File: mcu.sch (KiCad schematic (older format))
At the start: 37 parts, among them J10 DX07S016JA1R1500, J11 Conn_02x08_Odd_Even, J7 PD8-15 (digital), J8 PA0-7 (analog), J9 debug, U3 STM32F407VETx, Y1 8Mhz

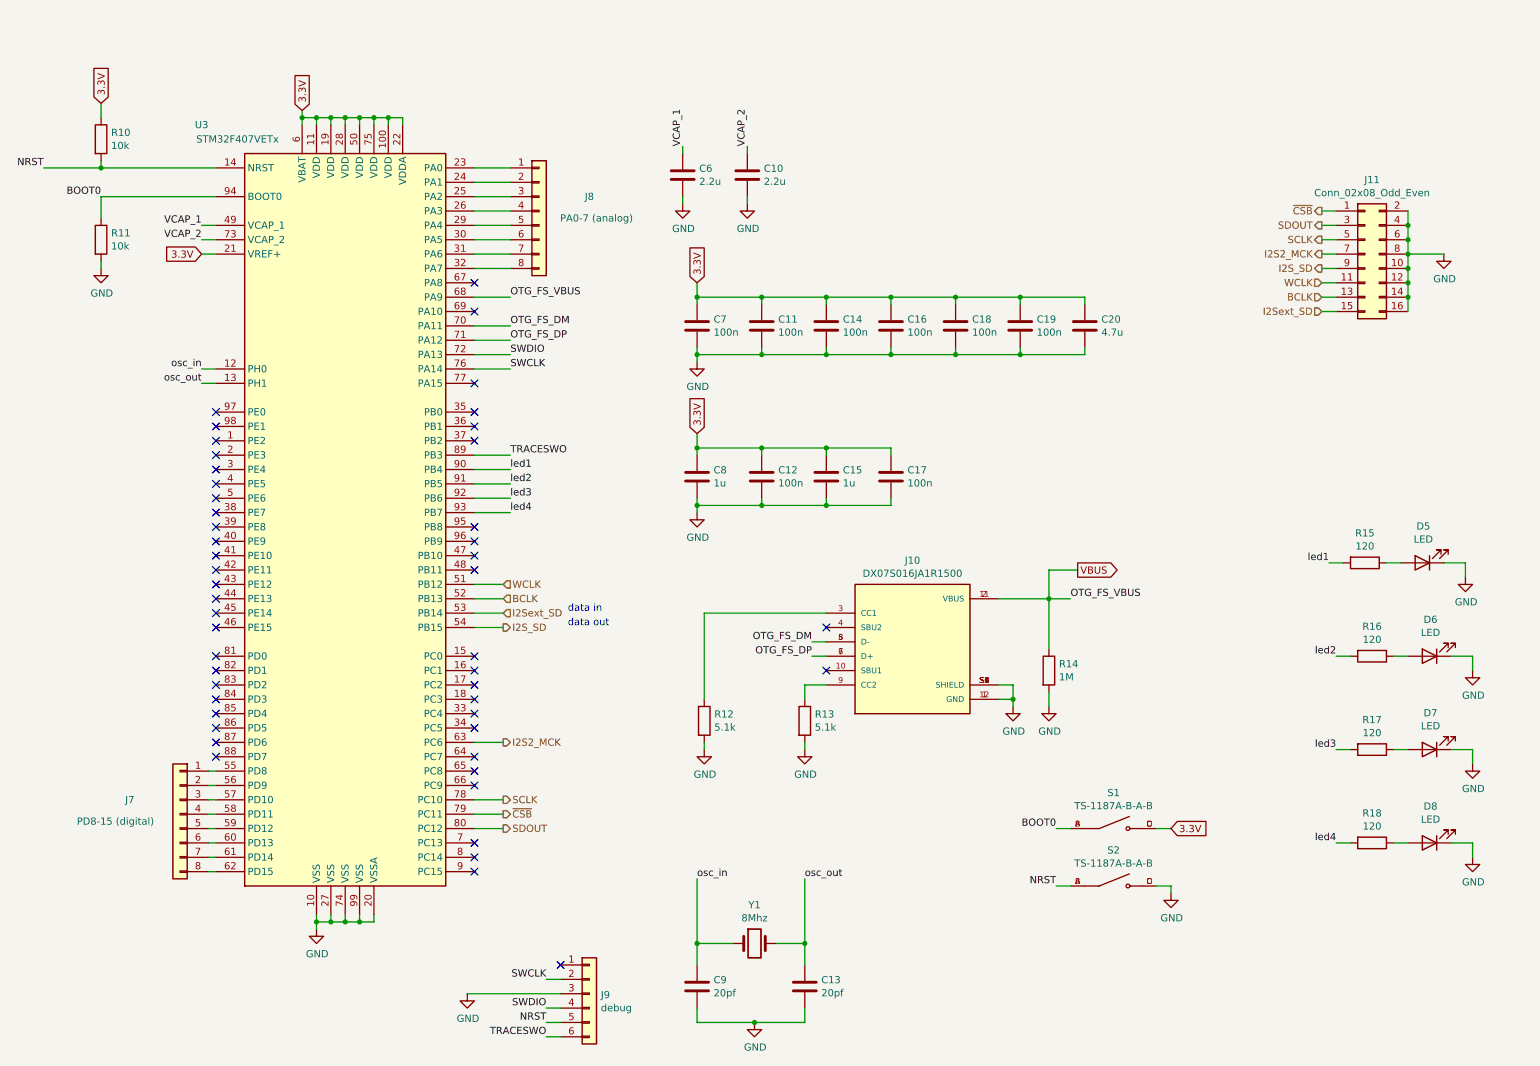
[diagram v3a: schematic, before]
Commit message: mcu.sch: replace microcontroller with SAME51J
The I2S bus is placed according to IOSET 1.

The ADC inputs are sprinkled around mostly-arbitrarily, but since
PA00-01 are not connected to either ADC peripheral, this uses PB08-09
for those two signals.  PB08 and 09 are connected to *both* ADCs, so
they should be sampleable simultaneously if necessary.
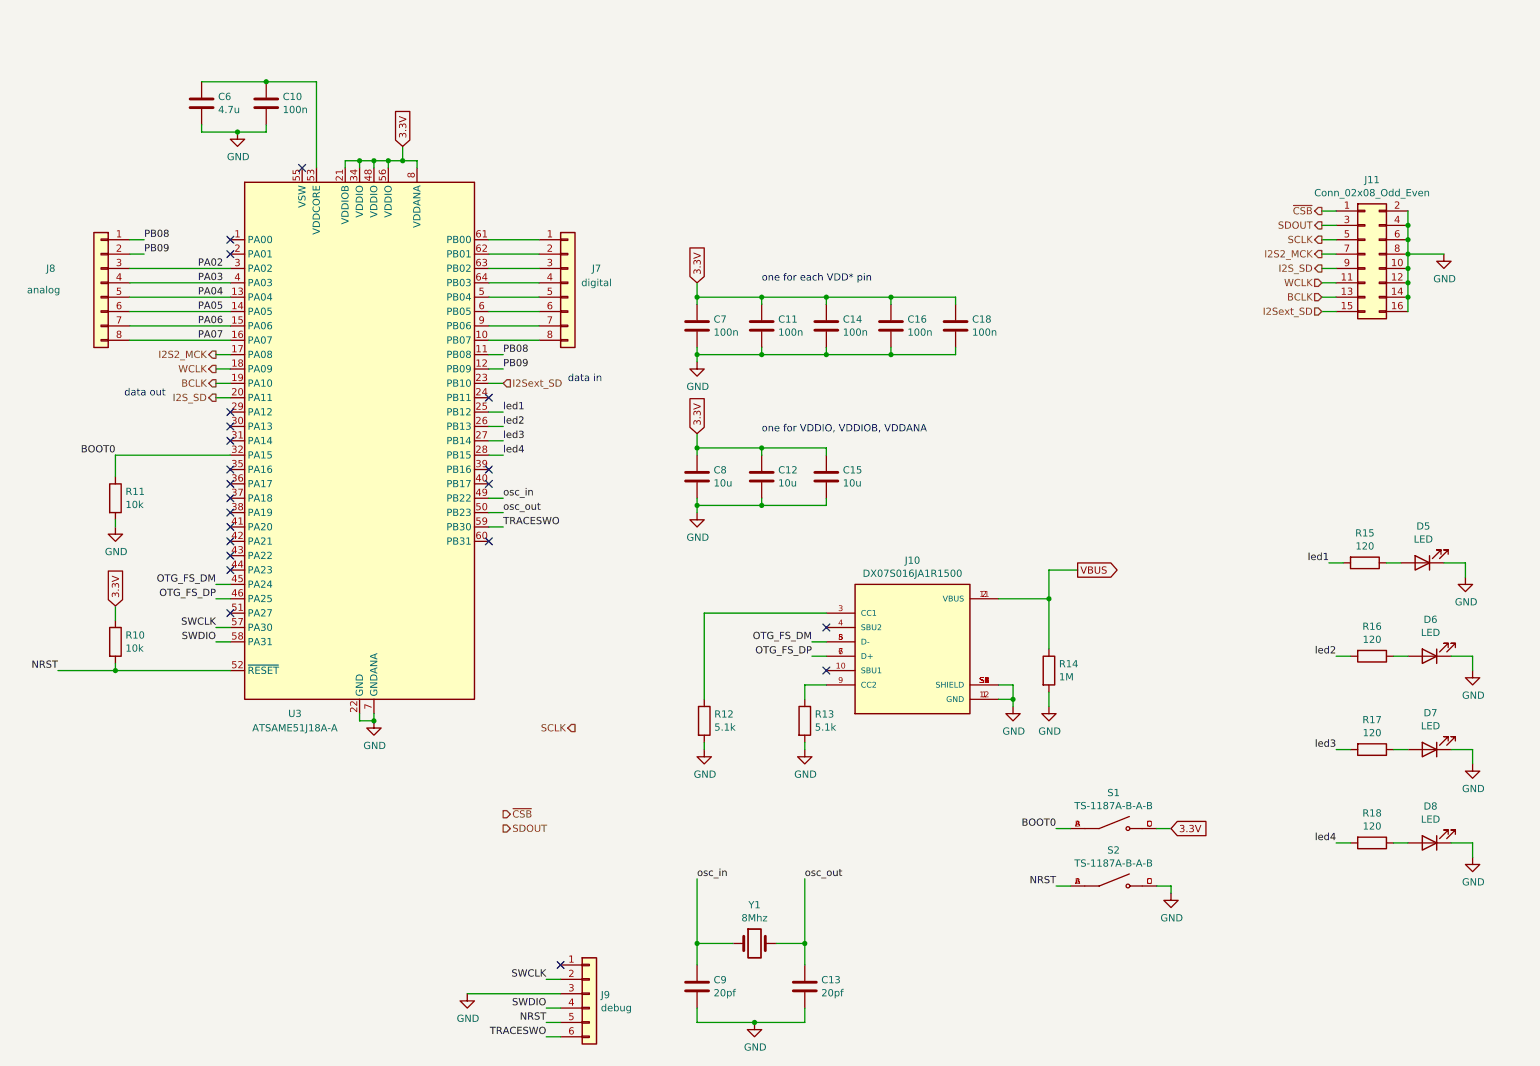
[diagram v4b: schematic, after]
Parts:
- removed C17, C19: 100n, Capacitor_SMD:C_0603_1608Metric, symbol Device:C
- removed C20: 4.7u, Capacitor_SMD:C_0603_1608Metric, symbol Device:C
- removed U3: STM32F407VETx, Package_QFP:LQFP-100_14x14mm_P0.5mm, symbol MCU_ST_STM32F4:STM32F407VETx
- added U3: ATSAME51J18A-A, Package_QFP:TQFP-64_10x10mm_P0.5mm, symbol MCU_Microchip_SAME:ATSAME51J18A-A
- C10: value 2.2u -> 100n; footprint Capacitor_SMD:C_0603_1608Metric -> (none)
- C12: value 100n -> 10u
- C15, C8: value 1u -> 10u
- C6: value 2.2u -> 4.7u; footprint Capacitor_SMD:C_0603_1608Metric -> (none)
- J7: value PD8-15 (digital) -> digital
- J8: value PA0-7 (analog) -> analog
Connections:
- net VCAP_2 is gone; now on an unnamed net: C10.1
- net 3.3V: now also U3.21 (VDDIOB), U3.34 (VDDIO), U3.48 (VDDIO), U3.56 (VDDIO), U3.8 (VDDANA)
- net BCLK: now also U3.19 (PA10)
- net BOOT0: now also U3.32 (PA15)
- net GND: now also U3.22 (GND), U3.33 (GND), U3.47 (GND), U3.54 (GND), U3.7 (GNDANA)
- net I2S2_MCK: now also U3.17 (PA08)
- net I2S_SD: now also U3.20 (PA11)
- net I2Sext_SD: now also U3.23 (PB10)
- net NRST: now also U3.52 (~RESET)
- net OTG_FS_DM: now also U3.45 (PA24)
- net OTG_FS_DP: now also U3.46 (PA25)
- net SWCLK: now also U3.57 (PA30)
- net SWDIO: now also U3.58 (PA31)
- net TRACESWO: now also U3.59 (PB30)
- net WCLK: now also U3.18 (PA09)
- net led1: now also U3.25 (PB12)
- net led2: now also U3.26 (PB13)
- net led3: now also U3.27 (PB14)
- net led4: now also U3.28 (PB15)
- net osc_in: now also U3.49 (PB22)
- net osc_out: now also U3.50 (PB23)
- net PB08: now reaches J8.1 (Pin_1)
- net PB08: now also U3.11 (PB08)
- net PB09: now reaches J8.2 (Pin_2)
- net PB09: now also U3.12 (PB09)
- net PA02: now reaches J8.3 (Pin_3)
- net PA02: now also U3.3 (PA02)
- net PA03: now reaches J8.4 (Pin_4)
- net PA03: now also U3.4 (PA03)
- net PA04: now reaches J8.5 (Pin_5)
- net PA04: now also U3.13 (PA04)
- net PA05: now reaches J8.6 (Pin_6)
- net PA05: now also U3.14 (PA05)
- net PA06: now reaches J8.7 (Pin_7)
- net PA06: now also U3.15 (PA06)
- net PA07: now reaches J8.8 (Pin_8)
- net PA07: now also U3.16 (PA07)
- net at J7.1 (Pin_1): now also U3.61 (PB00)
- net at J7.2 (Pin_2): now also U3.62 (PB01)
- net at J7.3 (Pin_3): now also U3.63 (PB02)
- net at J7.4 (Pin_4): now also U3.64 (PB03)
- net at J7.5 (Pin_5): now also U3.5 (PB04)
- net at J7.6 (Pin_6): now also U3.6 (PB05)
- net at J7.7 (Pin_7): now also U3.9 (PB06)
- net at J7.8 (Pin_8): now also U3.10 (PB07)
- net VCAP_1: no longer names the net of C6.1
- net VCAP_1: now also U3.53 (VDDCORE)
- no-connect marks 49 -> 22
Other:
- note added: "one for VDDIO, VDDIOB, VDDANA"
- note added: "one for each VDD* pin"
- moved on the sheet: J7, J8, R10, R11

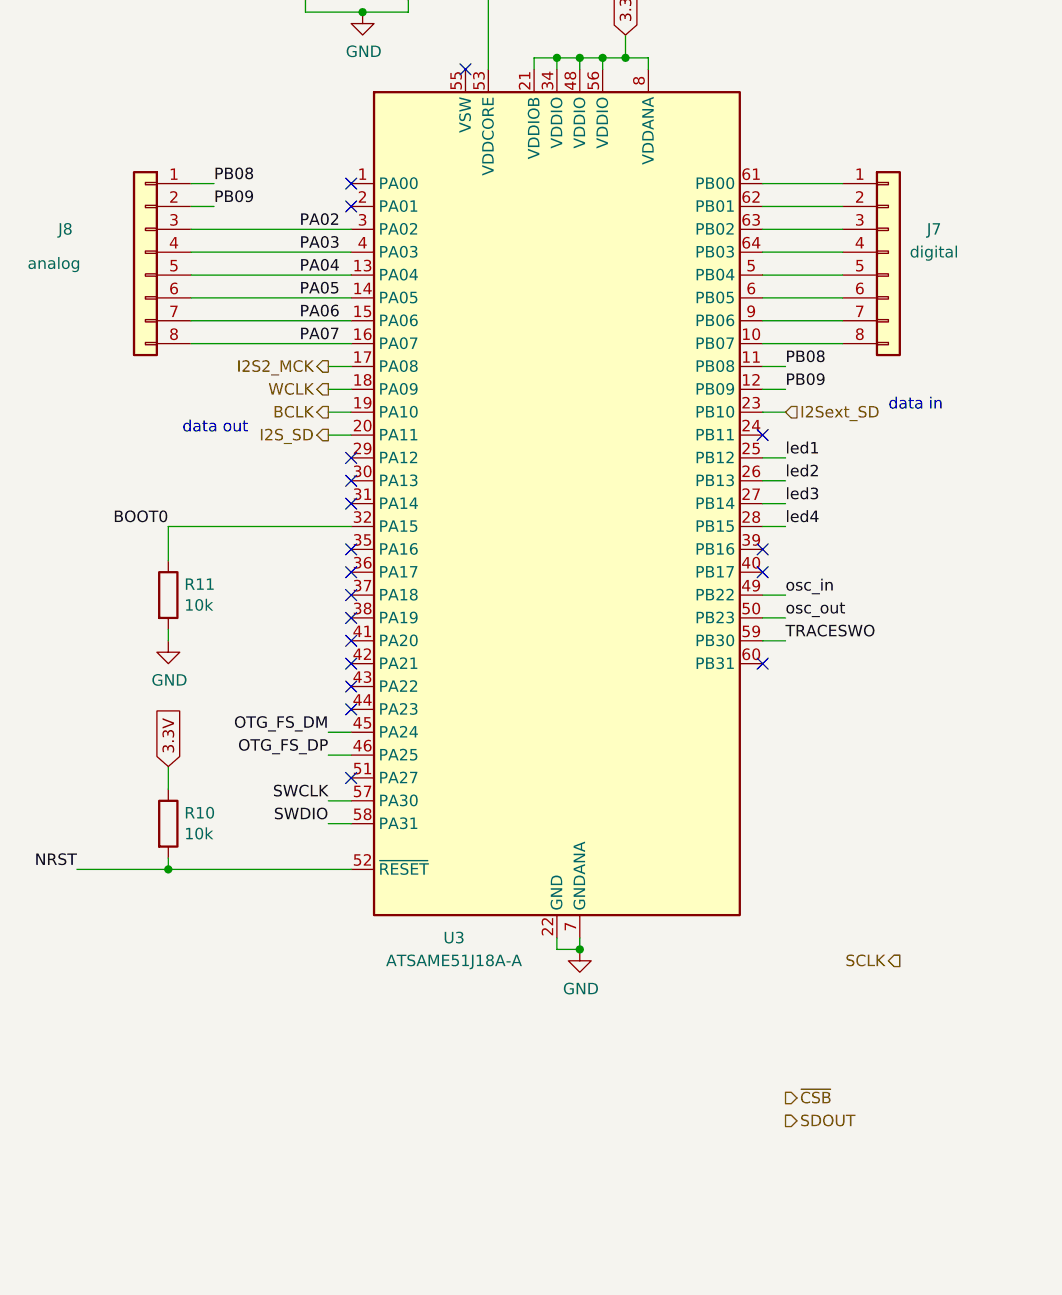
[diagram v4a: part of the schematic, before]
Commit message: Wire up SPI control, add TLV320AIC310x and I2C
The I2C is convenient: if I got it backwards, the SDA and SCL pins are
reversed between SERCOM 2 and 4.
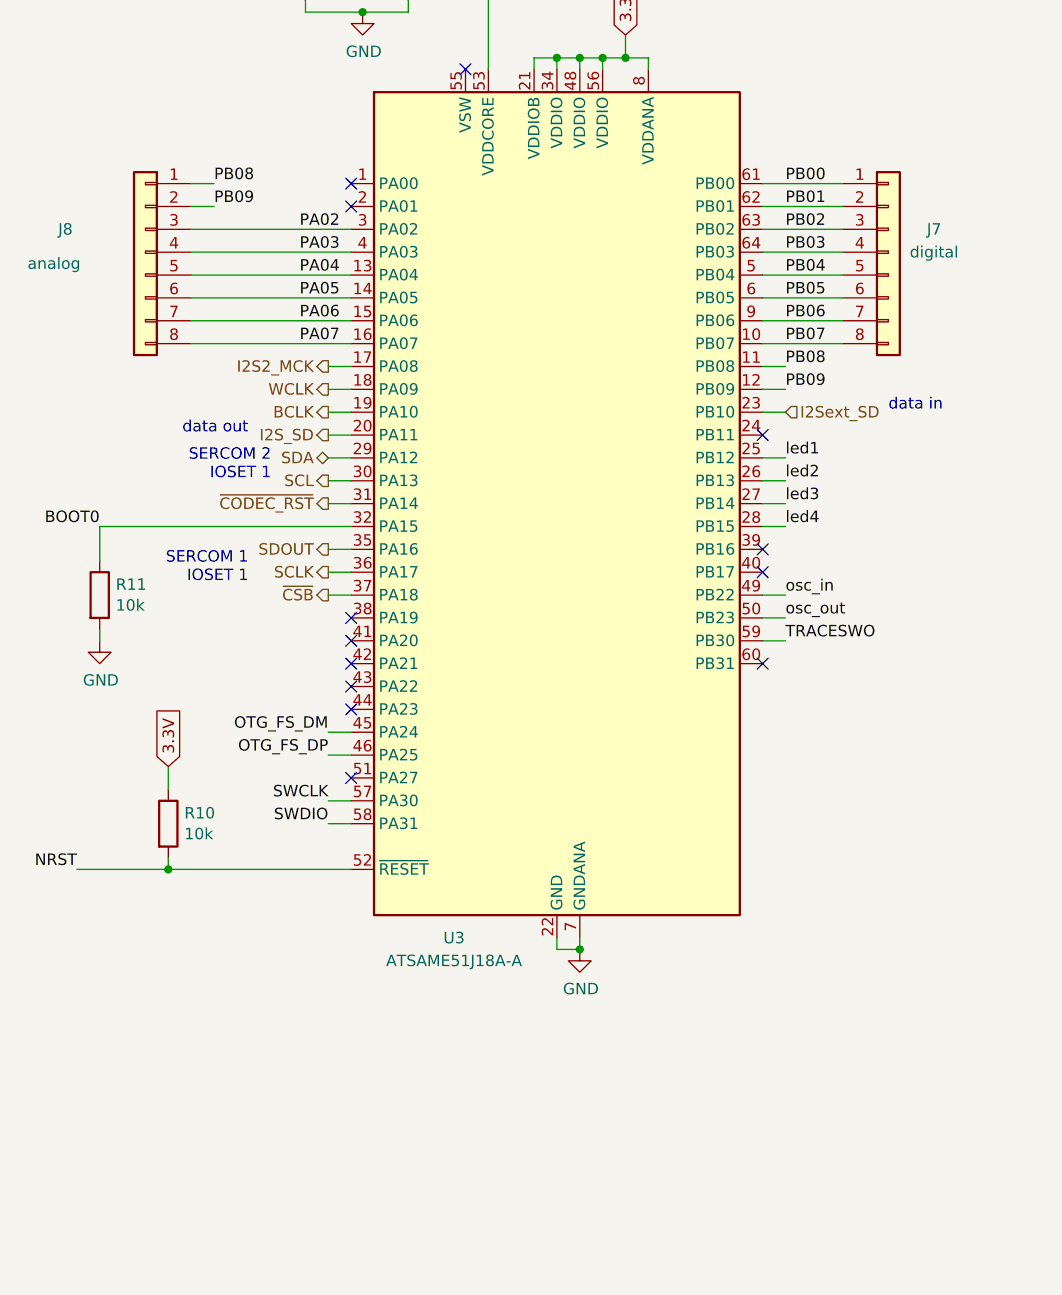
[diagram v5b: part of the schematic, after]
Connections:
- net SCLK: now also U3.36 (PA17)
- net SDOUT: now also U3.35 (PA16)
- net ~CSB: now also U3.37 (PA18)
- net PB00: now reaches J7.1 (Pin_1), U3.61 (PB00)
- net PB01: now reaches J7.2 (Pin_2), U3.62 (PB01)
- net PB02: now reaches J7.3 (Pin_3), U3.63 (PB02)
- net PB03: now reaches J7.4 (Pin_4), U3.64 (PB03)
- net PB04: now reaches J7.5 (Pin_5), U3.5 (PB04)
- net PB05: now reaches J7.6 (Pin_6), U3.6 (PB05)
- net PB06: now reaches J7.7 (Pin_7), U3.9 (PB06)
- net PB07: now reaches J7.8 (Pin_8), U3.10 (PB07)
- net SDA: now reaches U3.29 (PA12)
- net SCL: now reaches U3.30 (PA13)
- net ~CODEC_RST: now reaches U3.31 (PA14)
- no-connect marks 22 -> 16
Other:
- note added: "SERCOM 1\nIOSET 1"
- note added: "SERCOM 2\nIOSET 1"
- moved on the sheet: R11
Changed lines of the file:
@@
 $Descr A4 11693 8268
 encoding utf-8
-Sheet 2 3
+Sheet 2 4
 Title ""
 Date ""
@@
 $EndComp
 Wire Wire Line
-	1300 3200 2100 3200
-Text Label 1300 3200 2    50   ~ 0
+	1000 3200 2100 3200
+Text Label 1000 3200 2    50   ~ 0
 BOOT0
 Wire Wire Line
-	1300 3200 1300 3350
-Wire Wire Line
-	1300 3650 1300 3700
+	1000 3200 1000 3350
+Wire Wire Line
+	1000 3650 1000 3700
 $Comp
 L Device:R R11
 U 1 1 602B1BCD
-P 1300 3500
-F 0 "R11" H 1370 3546 50  0000 L CNN
-F 1 "10k" H 1370 3455 50  0000 L CNN
-F 2 "Resistor_SMD:R_0603_1608Metric" V 1230 3500 50  0001 C CNN
-F 3 "~" H 1300 3500 50  0001 C CNN
-	1    1300 3500
+P 1000 3500
+F 0 "R11" H 1070 3546 50  0000 L CNN
+F 1 "10k" H 1070 3455 50  0000 L CNN
+F 2 "Resistor_SMD:R_0603_1608Metric" V 930 3500 50  0001 C CNN
+F 3 "~" H 1000 3500 50  0001 C CNN
+	1    1000 3500
 	1    0    0    -1
 $EndComp
@@
 L power:GND #PWR016
 U 1 1 6007ECDF
-P 1300 3700
-F 0 "#PWR016" H 1300 3450 50  0001 C CNN
-F 1 "GND" H 1305 3527 50  0000 C CNN
-F 2 "" H 1300 3700 50  0001 C CNN
-F 3 "" H 1300 3700 50  0001 C CNN
-	1    1300 3700
+P 1000 3700
+F 0 "#PWR016" H 1000 3450 50  0001 C CNN
+F 1 "GND" H 1005 3527 50  0000 C CNN
+F 2 "" H 1000 3700 50  0001 C CNN
+F 3 "" H 1000 3700 50  0001 C CNN
+	1    1000 3700
 	1    0    0    -1
 $EndComp
@@
 Text GLabel 3300 1050 1    50   Input ~ 0
 3.3V
-Text HLabel 4000 5800 2    50   Output ~ 0
+Text HLabel 2000 3300 0    50   Output ~ 0
 SDOUT
-Text HLabel 4000 5700 2    50   Output ~ 0
+Text HLabel 2000 3500 0    50   Output ~ 0
 ~CSB
-Text HLabel 4500 5100 0    50   Output ~ 0
+Text HLabel 2000 3400 0    50   Output ~ 0
 SCLK
 Text Label 4000 3700 0    50   ~ 0
@@
 NoConn ~ 2100 3700
 NoConn ~ 2100 3600
-NoConn ~ 2100 3500
-NoConn ~ 2100 3400
-NoConn ~ 2100 3300
-NoConn ~ 2100 2900
-NoConn ~ 2100 3000
-NoConn ~ 2100 3100
 NoConn ~ 2100 1700
 NoConn ~ 2100 1800
@@
 NoConn ~ 3900 3400
 NoConn ~ 3900 3800
+Wire Wire Line
+	2100 3400 2000 3400
+Wire Wire Line
+	2000 3500 2100 3500
+Wire Wire Line
+	2100 3300 2000 3300
+Text Notes 1650 3450 2    50   ~ 0
+SERCOM 1\nIOSET 1
+Text HLabel 2000 2900 0    50   BiDi ~ 0
+SDA
+Text HLabel 2000 3000 0    50   Output ~ 0
+SCL
+Wire Wire Line
+	2000 2900 2100 2900
+Wire Wire Line
+	2100 3000 2000 3000
+Text HLabel 2000 3100 0    50   Output ~ 0
+~CODEC_RST
+Wire Wire Line
+	2100 3100 2000 3100
+Text Label 4000 1700 0    50   ~ 0
+PB00
+Text Label 4000 1800 0    50   ~ 0
+PB01
+Text Label 4000 1900 0    50   ~ 0
+PB02
+Text Label 4000 2000 0    50   ~ 0
+PB03
+Text Label 4000 2100 0    50   ~ 0
+PB04
+Text Label 4000 2200 0    50   ~ 0
+PB05
+Text Label 4000 2300 0    50   ~ 0
+PB06
+Text Label 4000 2400 0    50   ~ 0
+PB07
+Text Notes 1750 3000 2    50   ~ 0
+SERCOM 2\nIOSET 1
 $EndSCHEMATC

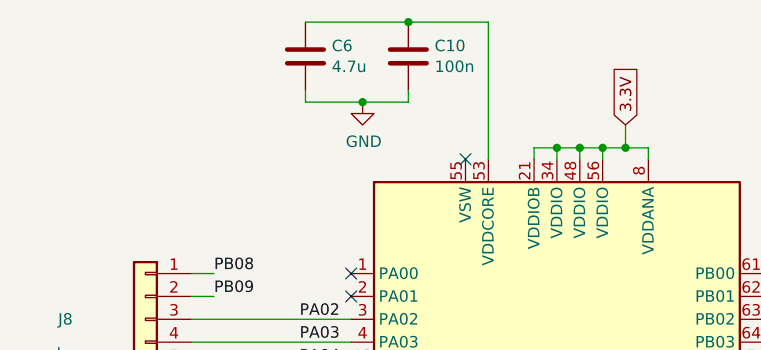
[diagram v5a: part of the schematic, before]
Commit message: mcu: swap 4.7u VDDCORE cap (C6) for 10u
There's already 10u all over the board so why not squeeze a bit more out
of the BOM.

Also adds a footprint for the 100n next to it (C10).
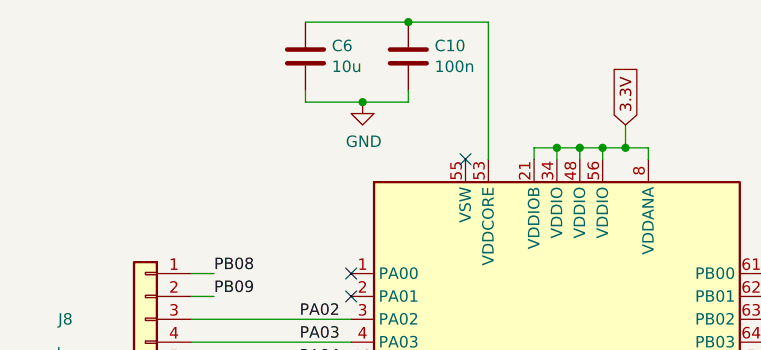
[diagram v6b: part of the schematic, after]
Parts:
- C10: footprint (none) -> Capacitor_SMD:C_0603_1608Metric
- C6: value 4.7u -> 10u; footprint (none) -> Capacitor_SMD:C_0603_1608Metric
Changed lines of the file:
@@
 P 1900 750
 F 0 "C6" H 2015 796 50  0000 L CNN
-F 1 "4.7u" H 2015 705 50  0000 L CNN
-F 2 "" H 1938 600 50  0001 C CNN
+F 1 "10u" H 2015 705 50  0000 L CNN
+F 2 "Capacitor_SMD:C_0603_1608Metric" H 1938 600 50  0001 C CNN
 F 3 "~" H 1900 750 50  0001 C CNN
 	1    1900 750
@@
 F 0 "C10" H 2465 796 50  0000 L CNN
 F 1 "100n" H 2465 705 50  0000 L CNN
-F 2 "" H 2388 600 50  0001 C CNN
+F 2 "Capacitor_SMD:C_0603_1608Metric" H 2388 600 50  0001 C CNN
 F 3 "~" H 2350 750 50  0001 C CNN
 	1    2350 750

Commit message: Apply footprint-finder's suggestion for USB-C
It likes the USB_C: prefix, I guess.
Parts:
- J10: footprint JAE_DX07S016JA1R1500 -> USB_C:JAE_DX07S016JA1R1500
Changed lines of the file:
@@
 F 0 "J10" H 6850 5067 50  0000 C CNN
 F 1 "DX07S016JA1R1500" H 6850 4976 50  0000 C CNN
-F 2 "JAE_DX07S016JA1R1500" H 6850 4500 50  0001 L BNN
+F 2 "USB_C:JAE_DX07S016JA1R1500" H 6850 4500 50  0001 L BNN
 F 3 "" H 6850 4500 50  0001 L BNN
 F 4 "3.31 mm" H 6850 4500 50  0001 L BNN "MAXIMUM_PACKAGE_HEIGHT"
